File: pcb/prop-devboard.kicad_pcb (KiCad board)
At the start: 4 copper layers, 50.8 x 22.9 mm, 48 parts, among them CN1 STDC14, CN2 SM04B-SRSS-TB (LF)(SN), CN3 ZX-PH2.0-WT2P, CN4 SM04B-SRSS-TB (LF)(SN), J1 Conn_01x12, J2 Conn_01x16, J3 GT-USB-7010ASV, Q1 DMG3415U-7, SW1 SW_Push, U1 STM32G0B1CBT6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

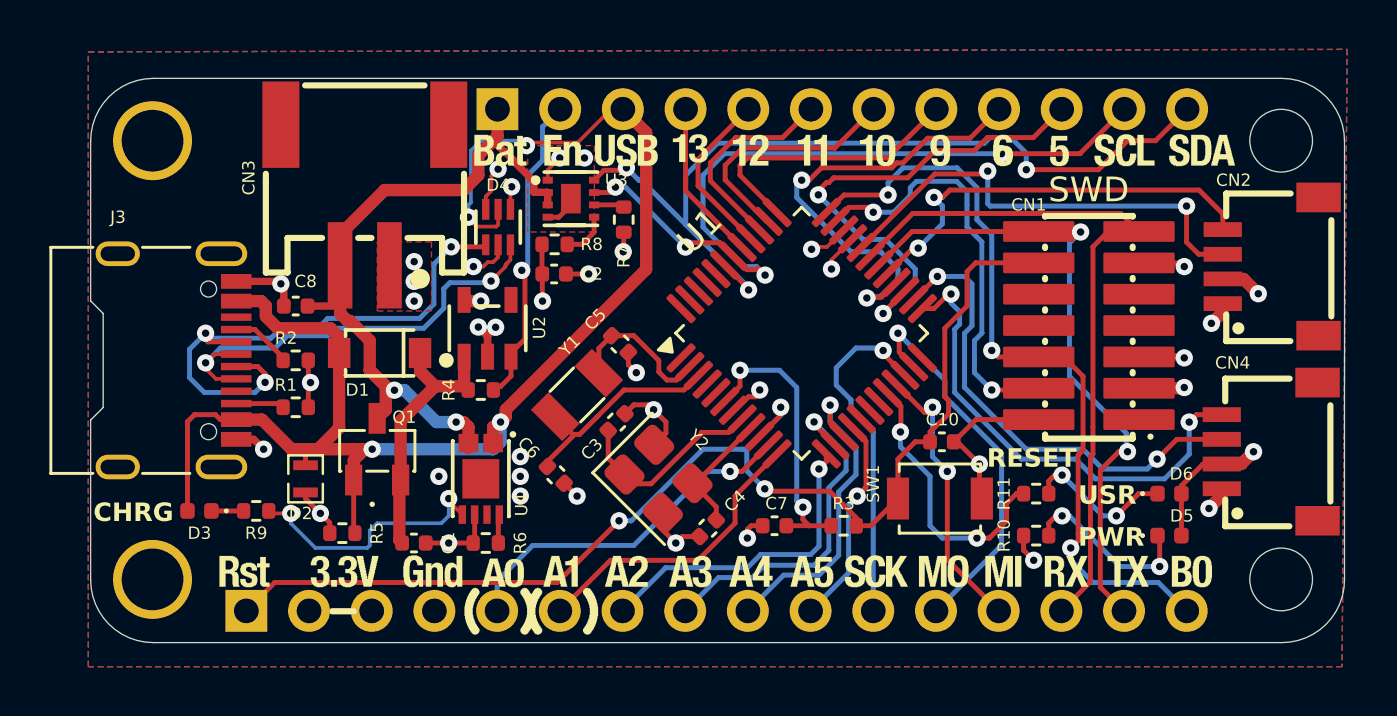
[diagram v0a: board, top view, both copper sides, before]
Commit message: Fixed various issues encountered during DFM checks
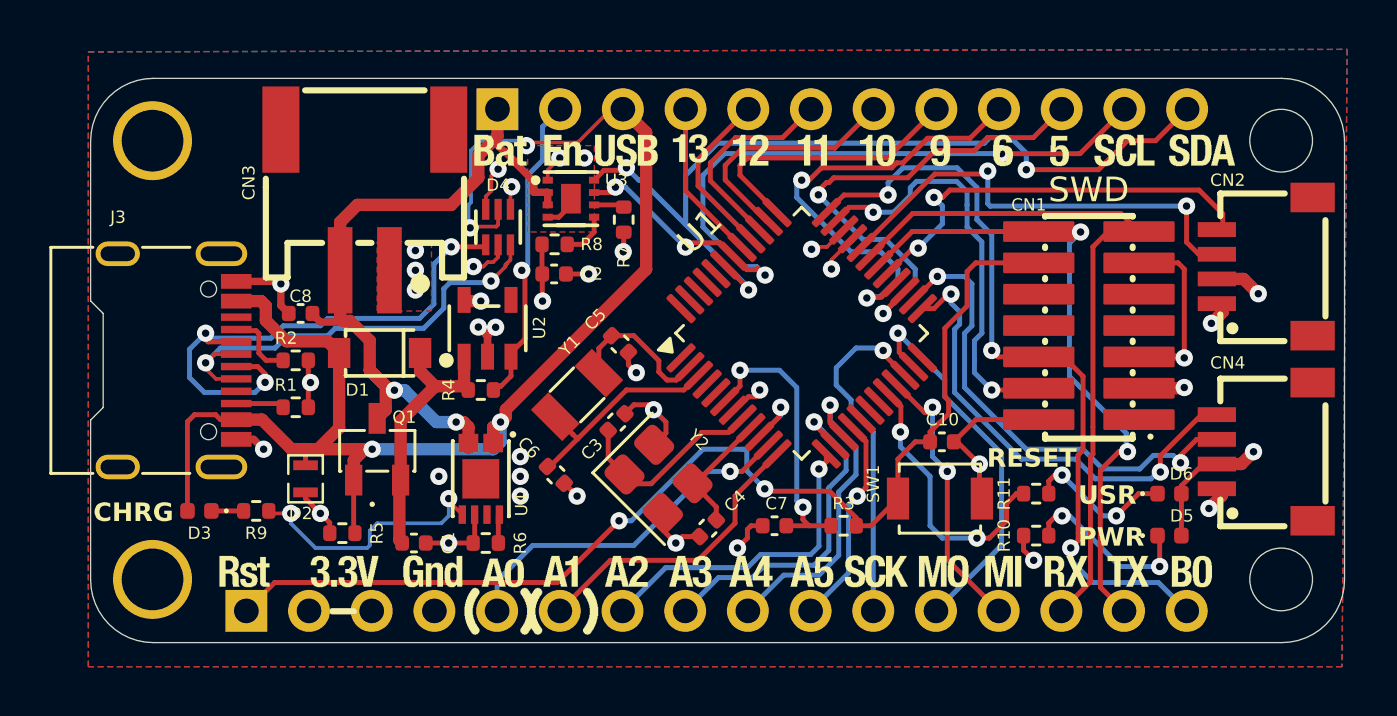
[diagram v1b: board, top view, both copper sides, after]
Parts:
- moved C8 0.36 mm to (108.6, 89.0)
- moved CN2 0.24 mm to (147.7, 87.1)
- moved CN4 0.20 mm to (147.7, 94.6)
- moved CN3 0.20 mm to (111.2, 84.4)
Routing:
- net GND: track 44.7 -> 49.3 mm, vias 31 -> 30
- net VBAT: track 30.6 -> 32.4 mm
- net I2C2_SCL: track 19.7 -> 19.2 mm

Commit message: Added silkscreen art to pcb
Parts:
- moved REF** 20.0 mm to (131.0, 93.9)
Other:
- board text added: "(c) CosmicSaturnArts"

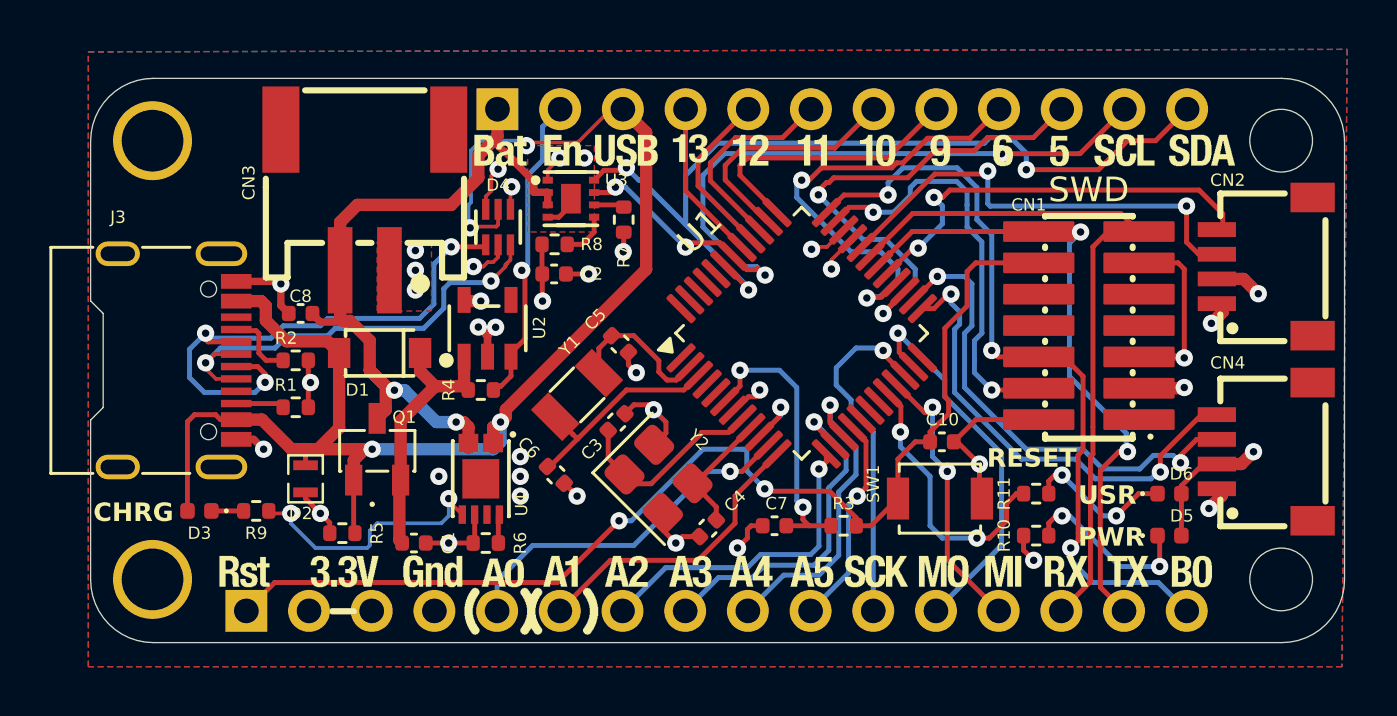
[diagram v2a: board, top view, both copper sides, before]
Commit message: Fixed MCU power pins not being connected correctly
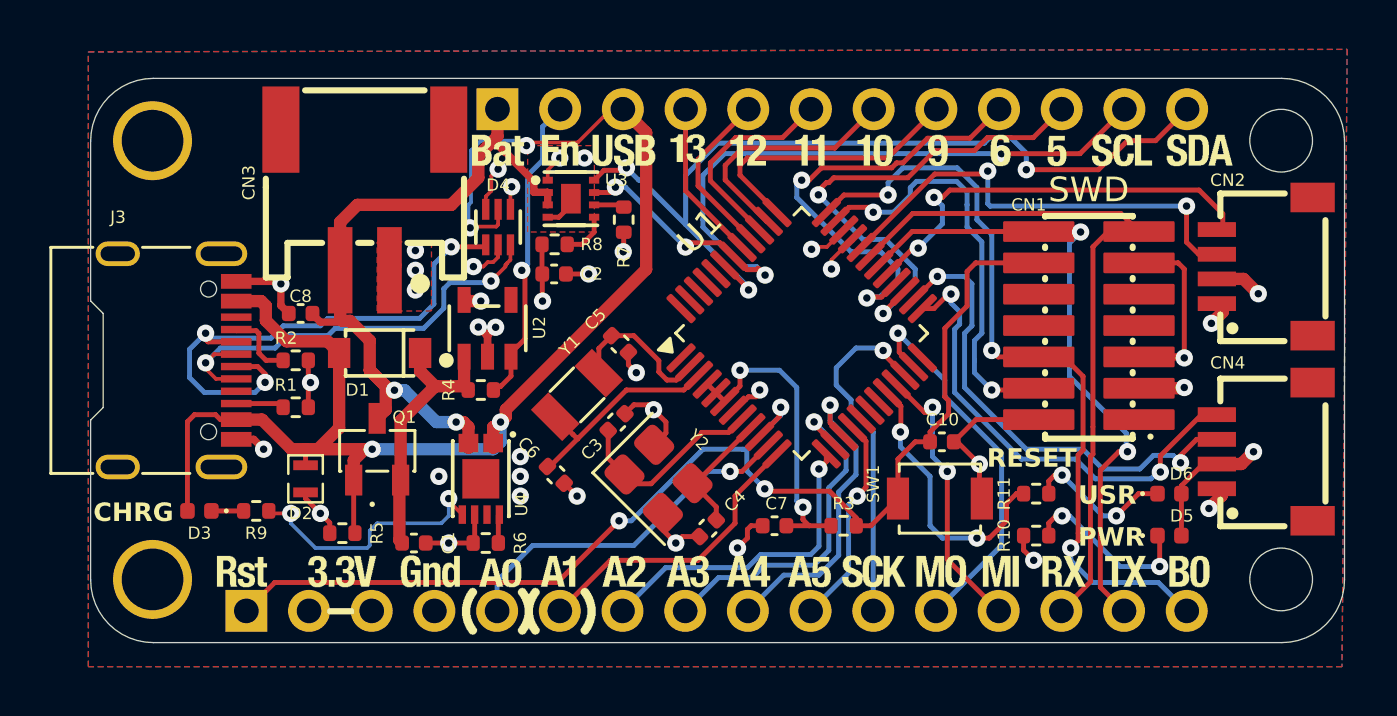
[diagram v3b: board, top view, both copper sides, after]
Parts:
- moved U$24 0.10 mm to (100.1, 102.3)
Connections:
- net BOOT0 renamed SWCLK/BOOT0
- U1 pad 4: unconnected-(U1-VBAT-Pad4) -> +3V3
- U1 pad 5: unconnected-(U1-VREF+-Pad5) -> +3V3
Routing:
- net +3V3: track 80.6 -> 81.6 mm
